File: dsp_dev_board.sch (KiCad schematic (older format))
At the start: 15 parts, among them U101 TL072, U102 AMS1117-3.3

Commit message: Add codec symbol
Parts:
- added U?: TLV320AIC3101, Package_DFN_QFN:QFN-32-1EP_5x5mm_P0.5mm_EP3.65x3.65mm, symbol Audio:TLV320AIC3101
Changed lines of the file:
@@
 Text Notes 900  4850 0    50   ~ 10
 Audio IO!
+$Comp
+L Audio:TLV320AIC3101 U?
+U 1 1 6002E047
+P 5600 4850
+F 0 "U?" H 4850 6300 50  0000 C CNN
+F 1 "TLV320AIC3101" H 5100 6200 50  0000 C CNN
+F 2 "Package_DFN_QFN:QFN-32-1EP_5x5mm_P0.5mm_EP3.65x3.65mm" H 5050 6150 50  0001 C CNN
+F 3 "https://www.ti.com/lit/ds/symlink/tlv320aic3101.pdf" H 5050 6150 50  0001 C CNN
+	1    5600 4850
+	1    0    0    -1
+$EndComp
 $EndSCHEMATC

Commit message: Wire up codec
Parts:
- removed U?: TLV320AIC3101, Package_DFN_QFN:QFN-32-1EP_5x5mm_P0.5mm_EP3.65x3.65mm, symbol Audio:TLV320AIC3101
- added C2, C3: 1u, symbol Device:C
- added R1, R2, R3, R4, R5, R6: 10k, symbol Device:R
- added U1: TL072, symbol Amplifier_Operational:TL072
- gave numbers to parts that had none: 5
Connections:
- net labels added: 4.5V, jack_in, jack_out
- wire segments 41 -> 72
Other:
- moved on the sheet: C101, D101, D102, J2, J3, R101, U101A

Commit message: Hook up peripherals
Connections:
- wire segments 72 -> 80
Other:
- moved on the sheet: C101, C2, C3, D101, D102, J2, J3, R101, R3, R4, R5, R6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

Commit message: Use a better codec
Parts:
- removed C102, C103: 0.1u, symbol Device:C
- removed R102: 3.3k, symbol Device:R
- removed R103: 10k, symbol Device:R
- removed U2: LM317A, Package_TO_SOT_SMD:TO-252-2, symbol Regulator_Linear:LM317A
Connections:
- net labels removed: 1.8V
- wire segments 80 -> 65
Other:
- note removed: "audio dev board"
- moved on the sheet: R1, R2, U1C

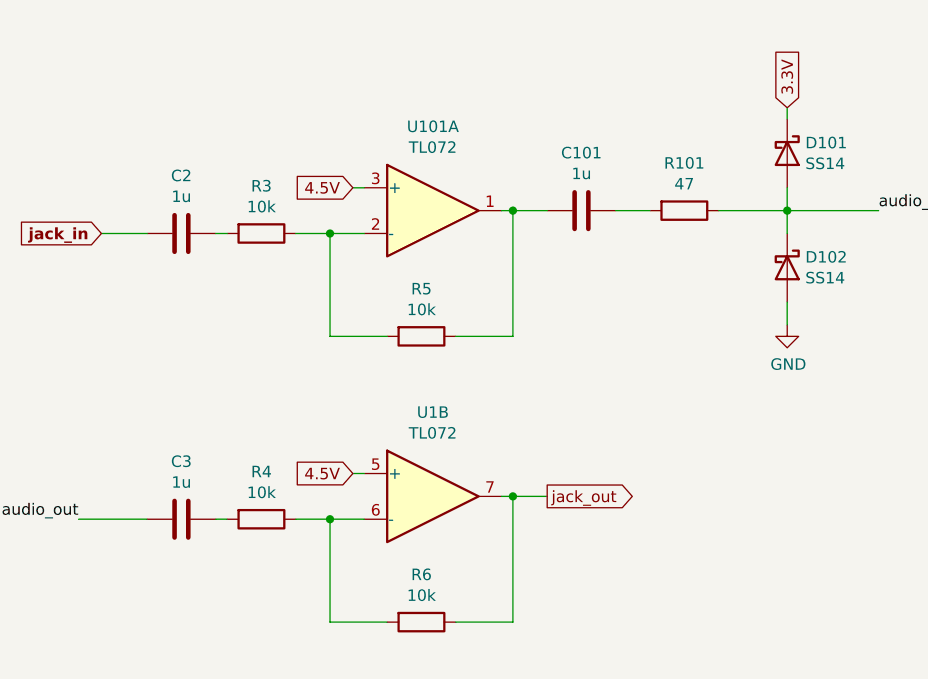
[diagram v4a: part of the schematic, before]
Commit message: Coupling caps, crystals
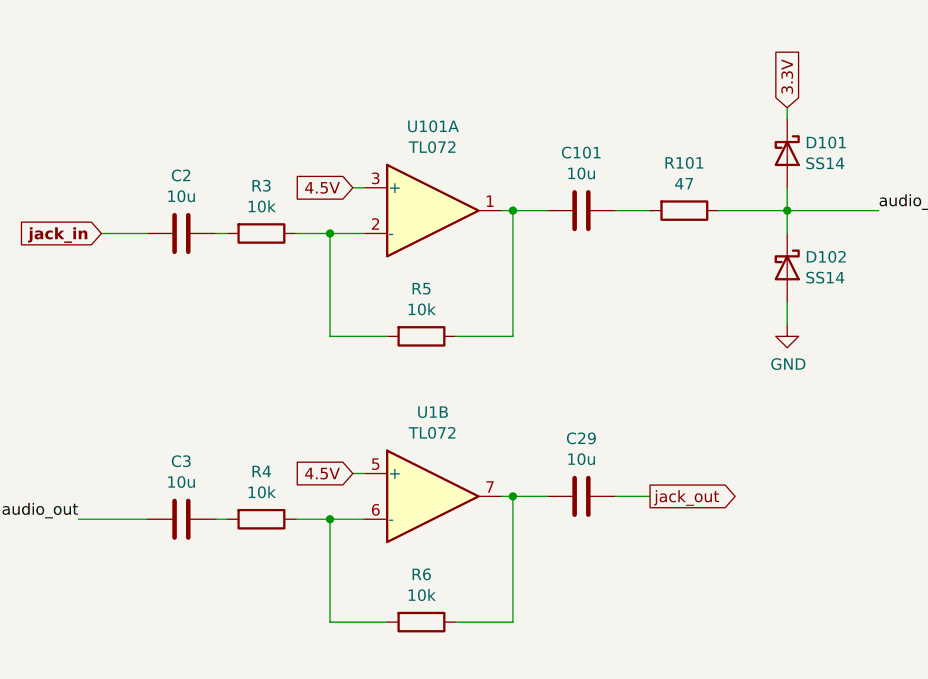
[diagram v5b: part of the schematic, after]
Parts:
- added C29: 10u, symbol Device:C
- C101, C2, C3: value 1u -> 10u
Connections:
- net jack_out: now also C29.1; no longer R6.1, U1.7
- new net: C29.2, R6.1, U1.7
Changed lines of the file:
@@
 P 8950 1800
 F 0 "C101" V 8698 1800 50  0000 C CNN
-F 1 "1u" V 8789 1800 50  0000 C CNN
+F 1 "10u" V 8789 1800 50  0000 C CNN
 F 2 "" H 8988 1650 50  0001 C CNN
 F 3 "~" H 8950 1800 50  0001 C CNN
@@
 P 7200 1900
 F 0 "C2" V 6948 1900 50  0000 C CNN
-F 1 "1u" V 7039 1900 50  0000 C CNN
+F 1 "10u" V 7039 1900 50  0000 C CNN
 F 2 "" H 7238 1750 50  0001 C CNN
 F 3 "~" H 7200 1900 50  0001 C CNN
@@
 	7950 1700 8000 1700
 Wire Wire Line
-	8800 3050 8650 3050
+	9250 3050 9100 3050
 $Comp
 L Device:R R6
@@
 Wire Wire Line
 	8650 3600 8650 3050
-Connection ~ 8650 3050
 Wire Wire Line
 	8650 3050 8600 3050
@@
 P 7200 3150
 F 0 "C3" V 6948 3150 50  0000 C CNN
-F 1 "1u" V 7039 3150 50  0000 C CNN
+F 1 "10u" V 7039 3150 50  0000 C CNN
 F 2 "" H 7238 3000 50  0001 C CNN
 F 3 "~" H 7200 3150 50  0001 C CNN
@@
 Wire Wire Line
 	6750 3150 7050 3150
-Text GLabel 8800 3050 2    50   Output ~ 0
+Text GLabel 9250 3050 2    50   Output ~ 0
 jack_out
 Text Label 8600 4950 0    50   ~ 0
@@
 Wire Wire Line
 	6900 5700 7550 5700
+$Comp
+L Device:C C29
+U 1 1 600DC113
+P 8950 3050
+F 0 "C29" V 8698 3050 50  0000 C CNN
+F 1 "10u" V 8789 3050 50  0000 C CNN
+F 2 "" H 8988 2900 50  0001 C CNN
+F 3 "~" H 8950 3050 50  0001 C CNN
+	1    8950 3050
+	0    1    1    0
+$EndComp
+Wire Wire Line
+	8800 3050 8650 3050
+Connection ~ 8650 3050
 $EndSCHEMATC

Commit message: Clean things up, add LEDs, aux stuff
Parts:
- removed J2, J3: AudioJack2, symbol Connector:AudioJack2
- added J2: aux_mcu_power, symbol Connector:Conn_01x02_Male
- added J3: input_jack, Connector_Audio:Jack_6.35mm_Neutrik_NMJ4HCD2_Horizontal, symbol Connector:AudioJack2_Switch
- added J7: output_jack, Connector_Audio:Jack_6.35mm_Neutrik_NMJ4HCD2_Horizontal, symbol Connector:AudioJack2_Switch
- added J8: audio_in, symbol Connector:Conn_01x02_Male
- added J9: audio_out, symbol Connector:Conn_01x02_Male
- J1: value Barrel_Jack -> 9v_jack
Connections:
- net 3.3V: now also J2.1 (Pin_1)
- net GND: now also J2.2 (Pin_2), J3.S, J7.S, J8.2 (Pin_2), J9.2 (Pin_2)
- net jack_in renamed audio_jack_in
- net audio_jack_in: now also J3.T, J8.1 (Pin_1)
- net jack_out renamed audio_jack_out
- net audio_jack_out: now also J7.T, J9.1 (Pin_1)
- no-connect marks 0 -> 4
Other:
- moved on the sheet: C1, U102

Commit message: USB
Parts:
- added D?: SS14, symbol Device:D_Schottky
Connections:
- net 9V: now also D?.1 (K)
- new net VBUS: D?.2 (A)
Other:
- moved on the sheet: R1, R2, U1C
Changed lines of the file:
@@
 Wire Wire Line
 	6850 1900 7050 1900
-Text GLabel 2700 3400 1    50   Input ~ 0
+Text GLabel 4550 3500 1    50   Input ~ 0
 9V
 $Comp
 L Device:R R1
 U 1 1 600A09B1
-P 2700 3700
-F 0 "R1" H 2770 3746 50  0000 L CNN
-F 1 "10k" H 2770 3655 50  0000 L CNN
-F 2 "" V 2630 3700 50  0001 C CNN
-F 3 "~" H 2700 3700 50  0001 C CNN
-	1    2700 3700
+P 4550 3800
+F 0 "R1" H 4620 3846 50  0000 L CNN
+F 1 "10k" H 4620 3755 50  0000 L CNN
+F 2 "" V 4480 3800 50  0001 C CNN
+F 3 "~" H 4550 3800 50  0001 C CNN
+	1    4550 3800
 	1    0    0    -1
 $EndComp
@@
 L Device:R R2
 U 1 1 600A106D
-P 2700 4150
-F 0 "R2" H 2770 4196 50  0000 L CNN
-F 1 "10k" H 2770 4105 50  0000 L CNN
-F 2 "" V 2630 4150 50  0001 C CNN
-F 3 "~" H 2700 4150 50  0001 C CNN
-	1    2700 4150
-	1    0    0    -1
-$EndComp
-Wire Wire Line
-	2700 3850 2700 3950
+P 4550 4250
+F 0 "R2" H 4620 4296 50  0000 L CNN
+F 1 "10k" H 4620 4205 50  0000 L CNN
+F 2 "" V 4480 4250 50  0001 C CNN
+F 3 "~" H 4550 4250 50  0001 C CNN
+	1    4550 4250
+	1    0    0    -1
+$EndComp
+Wire Wire Line
+	4550 3950 4550 4050
 $Comp
 L power:GND #PWR02
 U 1 1 600A2818
-P 2700 4400
-F 0 "#PWR02" H 2700 4150 50  0001 C CNN
-F 1 "GND" H 2705 4227 50  0000 C CNN
-F 2 "" H 2700 4400 50  0001 C CNN
-F 3 "" H 2700 4400 50  0001 C CNN
-	1    2700 4400
-	1    0    0    -1
-$EndComp
-Wire Wire Line
-	2700 4400 2700 4300
-Wire Wire Line
-	2700 3400 2700 3550
-Wire Wire Line
-	2700 3950 3050 3950
-Connection ~ 2700 3950
-Wire Wire Line
-	2700 3950 2700 4000
-Text GLabel 3050 3950 2    50   Output ~ 0
+P 4550 4500
+F 0 "#PWR02" H 4550 4250 50  0001 C CNN
+F 1 "GND" H 4555 4327 50  0000 C CNN
+F 2 "" H 4550 4500 50  0001 C CNN
+F 3 "" H 4550 4500 50  0001 C CNN
+	1    4550 4500
+	1    0    0    -1
+$EndComp
+Wire Wire Line
+	4550 4500 4550 4400
+Wire Wire Line
+	4550 3500 4550 3650
+Wire Wire Line
+	4550 4050 4900 4050
+Connection ~ 4550 4050
+Wire Wire Line
+	4550 4050 4550 4100
+Text GLabel 4900 4050 2    50   Output ~ 0
 4.5V
 Text GLabel 7950 1700 0    50   Input ~ 0
@@
 L Amplifier_Operational:TL072 U1
 U 3 1 600C8CB7
-P 1900 3950
-F 0 "U1" H 1858 3996 50  0000 L CNN
-F 1 "TL072" H 1858 3905 50  0000 L CNN
-F 2 "" H 1900 3950 50  0001 C CNN
-F 3 "http://www.ti.com/lit/ds/symlink/tl071.pdf" H 1900 3950 50  0001 C CNN
-	3    1900 3950
-	1    0    0    -1
-$EndComp
-Text GLabel 1800 3500 1    50   Input ~ 0
+P 3750 4050
+F 0 "U1" H 3708 4096 50  0000 L CNN
+F 1 "TL072" H 3708 4005 50  0000 L CNN
+F 2 "" H 3750 4050 50  0001 C CNN
+F 3 "http://www.ti.com/lit/ds/symlink/tl071.pdf" H 3750 4050 50  0001 C CNN
+	3    3750 4050
+	1    0    0    -1
+$EndComp
+Text GLabel 3650 3600 1    50   Input ~ 0
 9V
 Wire Wire Line
-	1800 3500 1800 3650
+	3650 3600 3650 3750
 $Comp
 L power:GND #PWR01
 U 1 1 600D21C7
-P 1800 4350
-F 0 "#PWR01" H 1800 4100 50  0001 C CNN
-F 1 "GND" H 1805 4177 50  0000 C CNN
-F 2 "" H 1800 4350 50  0001 C CNN
-F 3 "" H 1800 4350 50  0001 C CNN
-	1    1800 4350
-	1    0    0    -1
-$EndComp
-Wire Wire Line
-	1800 4350 1800 4250
+P 3650 4450
+F 0 "#PWR01" H 3650 4200 50  0001 C CNN
+F 1 "GND" H 3655 4277 50  0000 C CNN
+F 2 "" H 3650 4450 50  0001 C CNN
+F 3 "" H 3650 4450 50  0001 C CNN
+	1    3650 4450
+	1    0    0    -1
+$EndComp
+Wire Wire Line
+	3650 4450 3650 4350
 Wire Wire Line
 	6900 5150 7550 5150
@@
 Wire Wire Line
 	1750 2400 1650 2400
-Text GLabel 1650 2400 0    50   Input ~ 0
+Text GLabel 1450 2400 0    50   Input ~ 0
 9V
 Wire Wire Line
@@
 Wire Wire Line
 	2150 6950 2000 6950
+$Comp
+L Device:D_Schottky D?
+U 1 1 6020CE2E
+P 1350 2750
+F 0 "D?" H 1150 2900 50  0000 L CNN
+F 1 "SS14" H 1300 2900 50  0000 L CNN
+F 2 "" H 1350 2750 50  0001 C CNN
+F 3 "~" H 1350 2750 50  0001 C CNN
+	1    1350 2750
+	-1   0    0    1
+$EndComp
+Text GLabel 1050 2750 0    50   Input ~ 0
+VBUS
+Wire Wire Line
+	1500 2750 1650 2750
+Wire Wire Line
+	1650 2750 1650 2400
+Connection ~ 1650 2400
+Wire Wire Line
+	1650 2400 1450 2400
+Wire Wire Line
+	1200 2750 1050 2750
 $EndSCHEMATC

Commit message: Various fixes
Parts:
- added D6: SS14, symbol Device:D_Schottky
- added R14, R15: 1M, symbol Device:R
- gave numbers to parts that had none: 1
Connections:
- net 9V: now also D6.1 (K); no longer J1.1
- net GND: now also R14.2, R15.2
- net audio_jack_in: now also R14.1
- net audio_jack_out: now also R15.1
- new net: D6.2 (A), J1.1
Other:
- note removed: "Audio IO!"
- note removed: "Power!"
- moved on the sheet: J3, J7, R1, R2, U1C
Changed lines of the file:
@@
 	1    0    0    -1
 $EndComp
-Text GLabel 2500 1400 2    50   Output ~ 0
+Text GLabel 3050 1400 2    50   Output ~ 0
 9V
-Wire Wire Line
-	2500 1400 2350 1400
 $Comp
 L power:GND #PWR03
@@
 Wire Wire Line
 	2500 1600 2350 1600
-Text Notes 950  950  0    50   ~ 10
-Power!
 $Comp
 L power:GND #PWR05
 U 1 1 6002C64C
-P 4700 1500
-F 0 "#PWR05" H 4700 1250 50  0001 C CNN
-F 1 "GND" H 4705 1327 50  0000 C CNN
-F 2 "" H 4700 1500 50  0001 C CNN
-F 3 "" H 4700 1500 50  0001 C CNN
-	1    4700 1500
-	1    0    0    -1
-$EndComp
-Wire Wire Line
-	4700 1500 4700 1450
-Wire Wire Line
-	4700 1450 4500 1450
-Wire Wire Line
-	4500 1450 4500 1700
-Wire Wire Line
-	4500 1700 4400 1700
-Wire Wire Line
-	4500 1900 4400 1900
-Text Notes 3900 1150 0    50   ~ 10
-Audio IO!
+P 4700 1300
+F 0 "#PWR05" H 4700 1050 50  0001 C CNN
+F 1 "GND" H 4705 1127 50  0000 C CNN
+F 2 "" H 4700 1300 50  0001 C CNN
+F 3 "" H 4700 1300 50  0001 C CNN
+	1    4700 1300
+	1    0    0    -1
+$EndComp
+Wire Wire Line
+	4700 1300 4700 1250
+Wire Wire Line
+	4700 1250 4500 1250
+Wire Wire Line
+	4500 1250 4500 1500
+Wire Wire Line
+	4500 1500 4400 1500
+Wire Wire Line
+	4800 1700 4600 1700
 $Sheet
 S 6150 5000 750  1000
@@
 Wire Wire Line
 	6850 1900 7050 1900
-Text GLabel 4550 3500 1    50   Input ~ 0
+Text GLabel 2150 3500 1    50   Input ~ 0
 9V
 $Comp
 L Device:R R1
 U 1 1 600A09B1
-P 4550 3800
-F 0 "R1" H 4620 3846 50  0000 L CNN
-F 1 "10k" H 4620 3755 50  0000 L CNN
-F 2 "" V 4480 3800 50  0001 C CNN
-F 3 "~" H 4550 3800 50  0001 C CNN
-	1    4550 3800
+P 2150 3800
+F 0 "R1" H 2220 3846 50  0000 L CNN
+F 1 "10k" H 2220 3755 50  0000 L CNN
+F 2 "" V 2080 3800 50  0001 C CNN
+F 3 "~" H 2150 3800 50  0001 C CNN
+	1    2150 3800
 	1    0    0    -1
 $EndComp
@@
 L Device:R R2
 U 1 1 600A106D
-P 4550 4250
-F 0 "R2" H 4620 4296 50  0000 L CNN
-F 1 "10k" H 4620 4205 50  0000 L CNN
-F 2 "" V 4480 4250 50  0001 C CNN
-F 3 "~" H 4550 4250 50  0001 C CNN
-	1    4550 4250
-	1    0    0    -1
-$EndComp
-Wire Wire Line
-	4550 3950 4550 4050
+P 2150 4250
+F 0 "R2" H 2220 4296 50  0000 L CNN
+F 1 "10k" H 2220 4205 50  0000 L CNN
+F 2 "" V 2080 4250 50  0001 C CNN
+F 3 "~" H 2150 4250 50  0001 C CNN
+	1    2150 4250
+	1    0    0    -1
+$EndComp
+Wire Wire Line
+	2150 3950 2150 4050
 $Comp
 L power:GND #PWR02
 U 1 1 600A2818
-P 4550 4500
-F 0 "#PWR02" H 4550 4250 50  0001 C CNN
-F 1 "GND" H 4555 4327 50  0000 C CNN
-F 2 "" H 4550 4500 50  0001 C CNN
-F 3 "" H 4550 4500 50  0001 C CNN
-	1    4550 4500
-	1    0    0    -1
-$EndComp
-Wire Wire Line
-	4550 4500 4550 4400
-Wire Wire Line
-	4550 3500 4550 3650
-Wire Wire Line
-	4550 4050 4900 4050
-Connection ~ 4550 4050
-Wire Wire Line
-	4550 4050 4550 4100
-Text GLabel 4900 4050 2    50   Output ~ 0
+P 2150 4500
+F 0 "#PWR02" H 2150 4250 50  0001 C CNN
+F 1 "GND" H 2155 4327 50  0000 C CNN
+F 2 "" H 2150 4500 50  0001 C CNN
+F 3 "" H 2150 4500 50  0001 C CNN
+	1    2150 4500
+	1    0    0    -1
+$EndComp
+Wire Wire Line
+	2150 4500 2150 4400
+Wire Wire Line
+	2150 3500 2150 3650
+Wire Wire Line
+	2150 4050 2500 4050
+Connection ~ 2150 4050
+Wire Wire Line
+	2150 4050 2150 4100
+Text GLabel 2500 4050 2    50   Output ~ 0
 4.5V
 Text GLabel 7950 1700 0    50   Input ~ 0
@@
 L Amplifier_Operational:TL072 U1
 U 3 1 600C8CB7
-P 3750 4050
-F 0 "U1" H 3708 4096 50  0000 L CNN
-F 1 "TL072" H 3708 4005 50  0000 L CNN
-F 2 "" H 3750 4050 50  0001 C CNN
-F 3 "http://www.ti.com/lit/ds/symlink/tl071.pdf" H 3750 4050 50  0001 C CNN
-	3    3750 4050
-	1    0    0    -1
-$EndComp
-Text GLabel 3650 3600 1    50   Input ~ 0
+P 1600 4000
+F 0 "U1" H 1558 4046 50  0000 L CNN
+F 1 "TL072" H 1558 3955 50  0000 L CNN
+F 2 "" H 1600 4000 50  0001 C CNN
+F 3 "http://www.ti.com/lit/ds/symlink/tl071.pdf" H 1600 4000 50  0001 C CNN
+	3    1600 4000
+	1    0    0    -1
+$EndComp
+Text GLabel 1500 3550 1    50   Input ~ 0
 9V
 Wire Wire Line
-	3650 3600 3650 3750
+	1500 3550 1500 3700
 $Comp
 L power:GND #PWR01
 U 1 1 600D21C7
-P 3650 4450
-F 0 "#PWR01" H 3650 4200 50  0001 C CNN
-F 1 "GND" H 3655 4277 50  0000 C CNN
-F 2 "" H 3650 4450 50  0001 C CNN
-F 3 "" H 3650 4450 50  0001 C CNN
-	1    3650 4450
-	1    0    0    -1
-$EndComp
-Wire Wire Line
-	3650 4450 3650 4350
+P 1500 4400
+F 0 "#PWR01" H 1500 4150 50  0001 C CNN
+F 1 "GND" H 1505 4227 50  0000 C CNN
+F 2 "" H 1500 4400 50  0001 C CNN
+F 3 "" H 1500 4400 50  0001 C CNN
+	1    1500 4400
+	1    0    0    -1
+$EndComp
+Wire Wire Line
+	1500 4400 1500 4300
 Wire Wire Line
 	6900 5150 7550 5150
@@
 	8800 3050 8650 3050
 Connection ~ 8650 3050
-NoConn ~ 4400 1800
-NoConn ~ 4400 2000
-$Comp
-L Connector:AudioJack2_Switch J3
-U 1 1 601CE4FA
-P 4200 1900
-F 0 "J3" H 4100 2350 50  0000 C CNN
-F 1 "input_jack" H 4050 2250 50  0000 C CNN
-F 2 "Connector_Audio:Jack_6.35mm_Neutrik_NMJ4HCD2_Horizontal" H 4200 2100 50  0001 C CNN
-F 3 "~" H 4200 2100 50  0001 C CNN
-	1    4200 1900
-	1    0    0    -1
-$EndComp
+NoConn ~ 4400 1600
 $Comp
 L power:GND #PWR020
 U 1 1 601D9CA8
-P 4700 2200
-F 0 "#PWR020" H 4700 1950 50  0001 C CNN
-F 1 "GND" H 4705 2027 50  0000 C CNN
-F 2 "" H 4700 2200 50  0001 C CNN
-F 3 "" H 4700 2200 50  0001 C CNN
-	1    4700 2200
-	1    0    0    -1
-$EndComp
-Wire Wire Line
-	4700 2200 4700 2150
-Wire Wire Line
-	4700 2150 4500 2150
-Wire Wire Line
-	4500 2150 4500 2400
-Wire Wire Line
-	4500 2400 4400 2400
-Wire Wire Line
-	4500 2600 4400 2600
-NoConn ~ 4400 2500
-NoConn ~ 4400 2700
+P 4700 2450
+F 0 "#PWR020" H 4700 2200 50  0001 C CNN
+F 1 "GND" H 4705 2277 50  0000 C CNN
+F 2 "" H 4700 2450 50  0001 C CNN
+F 3 "" H 4700 2450 50  0001 C CNN
+	1    4700 2450
+	1    0    0    -1
+$EndComp
+Wire Wire Line
+	4700 2450 4700 2400
+Wire Wire Line
+	4700 2400 4500 2400
+Wire Wire Line
+	4500 2400 4500 2650
+Wire Wire Line
+	4500 2650 4400 2650
+NoConn ~ 4400 2750
 $Comp
 L Connector:AudioJack2_Switch J7
 U 1 1 601D9CB6
-P 4200 2600
-F 0 "J7" H 4100 3050 50  0000 C CNN
-F 1 "output_jack" H 4050 2950 50  0000 C CNN
-F 2 "Connector_Audio:Jack_6.35mm_Neutrik_NMJ4HCD2_Horizontal" H 4200 2800 50  0001 C CNN
-F 3 "~" H 4200 2800 50  0001 C CNN
-	1    4200 2600
-	1    0    0    -1
-$EndComp
-Text Label 4500 1900 0    50   ~ 0
+P 4200 2850
+F 0 "J7" H 4100 3300 50  0000 C CNN
+F 1 "output_jack" H 4050 3200 50  0000 C CNN
+F 2 "Connector_Audio:Jack_6.35mm_Neutrik_NMJ4HCD2_Horizontal" H 4200 3050 50  0001 C CNN
+F 3 "~" H 4200 3050 50  0001 C CNN
+	1    4200 2850
+	1    0    0    -1
+$EndComp
+Text Label 4800 1700 0    50   ~ 0
 audio_jack_in
-Text Label 4500 2600 0    50   ~ 0
+Text Label 4800 2850 0    50   ~ 0
 audio_jack_out
 Text Label 6850 1900 2    50   ~ 0
@@
 	2150 6950 2000 6950
 $Comp
-L Device:D_Schottky D?
+L Device:D_Schottky D5
 U 1 1 6020CE2E
 P 1350 2750
-F 0 "D?" H 1150 2900 50  0000 L CNN
+F 0 "D5" H 1150 2900 50  0000 L CNN
 F 1 "SS14" H 1300 2900 50  0000 L CNN
 F 2 "" H 1350 2750 50  0001 C CNN
@@
 Wire Wire Line
 	1200 2750 1050 2750
+$Comp
+L Connector:AudioJack2_Switch J3
+U 1 1 601CE4FA
+P 4200 1700
+F 0 "J3" H 4100 2150 50  0000 C CNN
+F 1 "input_jack" H 4050 2050 50  0000 C CNN
+F 2 "Connector_Audio:Jack_6.35mm_Neutrik_NMJ4HCD2_Horizontal" H 4200 1900 50  0001 C CNN
+F 3 "~" H 4200 1900 50  0001 C CNN
+	1    4200 1700
+	1    0    0    -1
+$EndComp
+$Comp
+L Device:R R14
+U 1 1 600E7C35
+P 4600 1850
+F 0 "R14" H 4670 1896 50  0000 L CNN
+F 1 "1M" H 4670 1805 50  0000 L CNN
+F 2 "" V 4530 1850 50  0001 C CNN
+F 3 "~" H 4600 1850 50  0001 C CNN
+	1    4600 1850
+	1    0    0    -1
+$EndComp
+$Comp
+L power:GND #PWR033
+U 1 1 600E8A0A
+P 4600 2050
+F 0 "#PWR033" H 4600 1800 50  0001 C CNN
+F 1 "GND" H 4605 1877 50  0000 C CNN
+F 2 "" H 4600 2050 50  0001 C CNN
+F 3 "" H 4600 2050 50  0001 C CNN
+	1    4600 2050
+	1    0    0    -1
+$EndComp
+Wire Wire Line
+	4600 2050 4600 2000
+$Comp
+L Device:R R15
+U 1 1 600EC6BA
+P 4600 3000
+F 0 "R15" H 4670 3046 50  0000 L CNN
+F 1 "1M" H 4670 2955 50  0000 L CNN
+F 2 "" V 4530 3000 50  0001 C CNN
+F 3 "~" H 4600 3000 50  0001 C CNN
+	1    4600 3000
+	1    0    0    -1
+$EndComp
+$Comp
+L power:GND #PWR034
+U 1 1 600EC6C0
+P 4600 3200
+F 0 "#PWR034" H 4600 2950 50  0001 C CNN
+F 1 "GND" H 4605 3027 50  0000 C CNN
+F 2 "" H 4600 3200 50  0001 C CNN
+F 3 "" H 4600 3200 50  0001 C CNN
+	1    4600 3200
+	1    0    0    -1
+$EndComp
+Wire Wire Line
+	4600 3200 4600 3150
+NoConn ~ 4400 1800
+NoConn ~ 4400 2950
+Wire Wire Line
+	4800 2850 4600 2850
+Connection ~ 4600 2850
+Wire Wire Line
+	4600 2850 4400 2850
+Wire Wire Line
+	4600 1700 4400 1700
+Connection ~ 4600 1700
+$Comp
+L Device:D_Schottky D6
+U 1 1 60286E4B
+P 2700 1400
+F 0 "D6" H 2550 1250 50  0000 L CNN
+F 1 "SS14" H 2700 1250 50  0000 L CNN
+F 2 "" H 2700 1400 50  0001 C CNN
+F 3 "~" H 2700 1400 50  0001 C CNN
+	1    2700 1400
+	-1   0    0    1
+$EndComp
+Wire Wire Line
+	3050 1400 2850 1400
+Wire Wire Line
+	2550 1400 2350 1400
 $EndSCHEMATC
